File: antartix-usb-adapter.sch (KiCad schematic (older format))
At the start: 120 parts, among them IC1 FT2232D, J1 QTE-020-04-L-D-A, J2 0022232041, J3 614004185023, J4 WE_629105150521, J5 614004185023, J6 614004185023, U1 PCT2075GVX, U2 PAC1934T-I_JQ, U3 USB2514B-I_M2, U4 TPS2024DR, U5 TPS2024DR, U6 TPS2024DR, Y1 7C-24.000MBB-T, Y2 MQ-6.000-12-30_30_

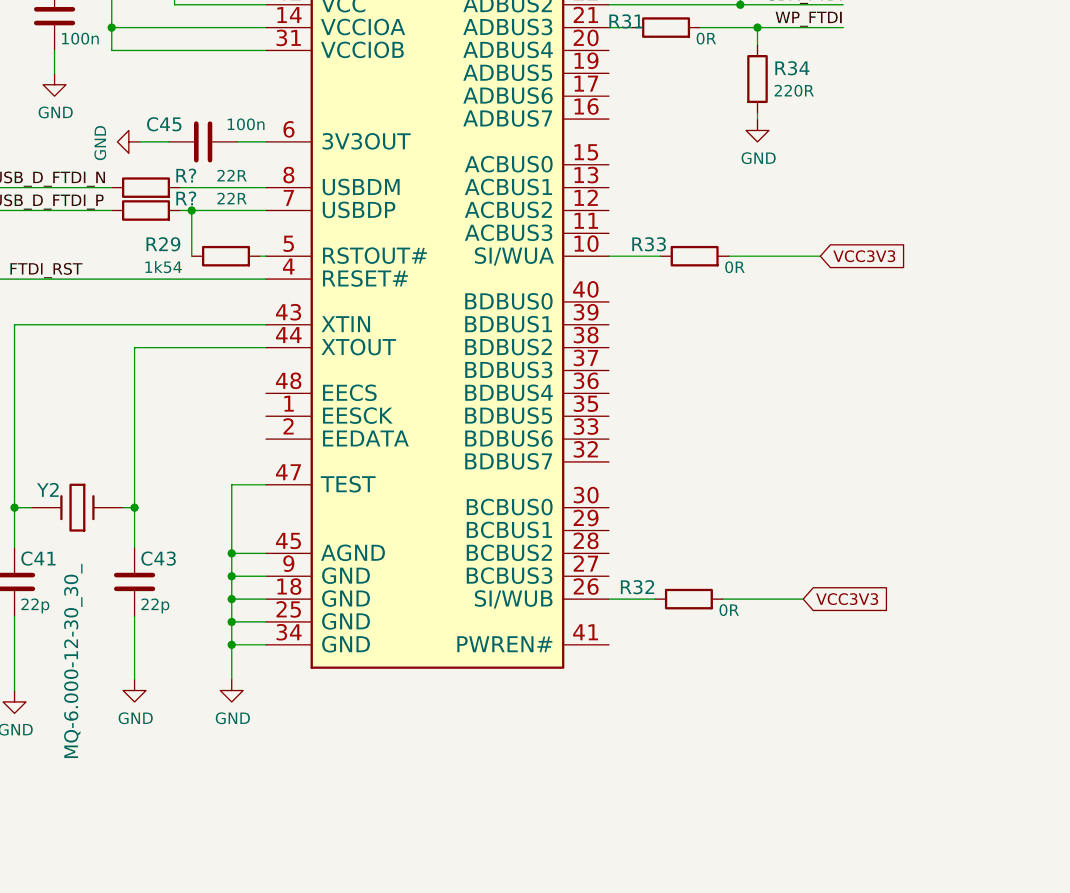
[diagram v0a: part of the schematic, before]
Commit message: Added micromatch-12 connector as PMOD GPIO. Bumped to 1.2.0
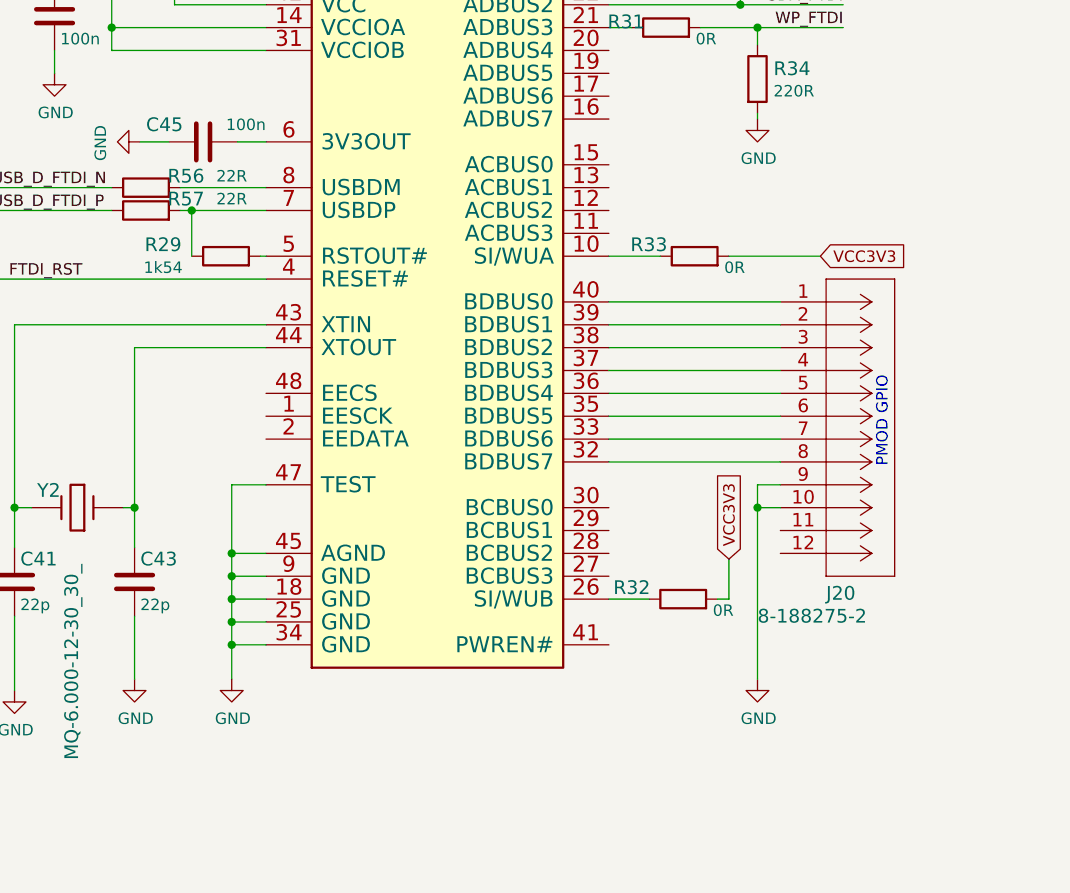
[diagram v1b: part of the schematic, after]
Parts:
- added J20: 8-188275-2, antartix-arty-controller-footprints:8-188275-2, symbol antartix-arty-controller:8-188275-2
- gave numbers to parts that had none: 2
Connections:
- net GND: now also J20.10, J20.9
- net at IC1.32 (BDBUS7): now also J20.8
- net at IC1.33 (BDBUS6): now also J20.7
- net at IC1.35 (BDBUS5): now also J20.6
- net at IC1.36 (BDBUS4): now also J20.5
- net at IC1.37 (BDBUS3): now also J20.4
- net at IC1.38 (BDBUS2): now also J20.3
- net at IC1.39 (BDBUS1): now also J20.2
- net at IC1.40 (BDBUS0): now also J20.1
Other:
- note added: "PMOD GPIO"
- moved on the sheet: R32
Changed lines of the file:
@@
 Title ""
 Date ""
-Rev ""
+Rev "1.2.0"
 Comp ""
 Comment1 ""
@@
 Wire Notes Line
 	11550 525  11550 11275
-Text GLabel 15575 9150 2    50   Input ~ 0
+Text GLabel 15250 8975 1    50   Input ~ 0
 VCC3V3
 Wire Wire Line
-	15225 9150 15575 9150
+	15250 9150 15250 8975
 $Comp
 L antartix-arty-controller:R_0R_0402 R?
 U 1 1 609392A5
-P 15075 9150
+P 15050 9150
 AR Path="/609392A5" Ref="R?"  Part="1"
 AR Path="/60924187/609392A5" Ref="R32"  Part="1"
-F 0 "R32" H 14850 9200 60  0000 C CNN
-F 1 "R_0R_0402" H 15075 9000 60  0001 C CNN
-F 2 "antartix-arty-controller-footprints:0402-res" H 15275 9350 60  0001 L CNN
-F 3 "" H 15075 9150 50  0001 C CNN
-F 4 "PANASONIC" H 15275 9550 60  0001 L CNN "Manufacturer"
-F 5 "ERJ2GE0R00X" H 15275 9450 60  0001 L CNN "MPN"
-F 6 "0R" H 15250 9100 50  0000 C CNN "Val"
-	1    15075 9150
+F 0 "R32" H 14825 9200 60  0000 C CNN
+F 1 "R_0R_0402" H 15050 9000 60  0001 C CNN
+F 2 "antartix-arty-controller-footprints:0402-res" H 15250 9350 60  0001 L CNN
+F 3 "" H 15050 9150 50  0001 C CNN
+F 4 "PANASONIC" H 15250 9550 60  0001 L CNN "Manufacturer"
+F 5 "ERJ2GE0R00X" H 15250 9450 60  0001 L CNN "MPN"
+F 6 "0R" H 15225 9100 50  0000 C CNN "Val"
+	1    15050 9150
 	1    0    0    -1
 $EndComp
 Wire Wire Line
-	14725 9150 14925 9150
+	14725 9150 14900 9150
 Text GLabel 9450 9225 1    50   Input ~ 0
 VCC3V3
@@
 P 12700 7350
 AR Path="/604C47E1/605E94E5" Ref="R?"  Part="1"
-AR Path="/60924187/605E94E5" Ref="R?"  Part="1"
-F 0 "R?" H 12875 7400 60  0000 C CNN
+AR Path="/60924187/605E94E5" Ref="R56"  Part="1"
+F 0 "R56" H 12875 7400 60  0000 C CNN
 F 1 "R_22R_0402" H 12700 7200 60  0001 C CNN
 F 2 "antartix-arty-controller-footprints:0402-res" H 12900 7550 60  0001 L CNN
@@
 P 12700 7450
 AR Path="/604C47E1/605E94EE" Ref="R?"  Part="1"
-AR Path="/60924187/605E94EE" Ref="R?"  Part="1"
-F 0 "R?" H 12875 7500 60  0000 C CNN
+AR Path="/60924187/605E94EE" Ref="R57"  Part="1"
+F 0 "R57" H 12875 7500 60  0000 C CNN
 F 1 "R_22R_0402" H 12700 7300 60  0001 C CNN
 F 2 "antartix-arty-controller-footprints:0402-res" H 12900 7650 60  0001 L CNN
@@
 Wire Wire Line
 	12550 7450 12025 7450
+$Comp
+L antartix-arty-controller:8-188275-2 J20
+U 1 1 6058E829
+P 15475 7850
+F 0 "J20" H 15675 6575 60  0000 L CNN
+F 1 "8-188275-2" H 15375 6475 60  0000 L CNN
+F 2 "antartix-arty-controller-footprints:8-188275-2" H 15875 7190 60  0001 C CNN
+F 3 "" H 15475 7850 60  0000 C CNN
+F 4 "8-188275-2" H 15850 8075 50  0001 C CNN "MPN"
+F 5 "TE Connectivity" H 15825 8000 50  0001 C CNN "Manufacturer"
+	1    15475 7850
+	1    0    0    -1
+$EndComp
+Wire Wire Line
+	14725 7850 15475 7850
+Wire Wire Line
+	14725 7950 15475 7950
+Wire Wire Line
+	14725 8050 15475 8050
+Wire Wire Line
+	14725 8150 15475 8150
+Wire Wire Line
+	14725 8250 15475 8250
+Wire Wire Line
+	14725 8350 15475 8350
+Wire Wire Line
+	14725 8450 15475 8450
+Wire Wire Line
+	14725 8550 15475 8550
+Wire Wire Line
+	15475 8650 15375 8650
+Wire Wire Line
+	15375 8650 15375 8750
+Wire Wire Line
+	15475 8750 15375 8750
+Connection ~ 15375 8750
+Wire Wire Line
+	15375 8750 15375 9500
+$Comp
+L antartix-arty-controller:GND #PWR?
+U 1 1 6084ADBB
+P 15375 9500
+AR Path="/6084ADBB" Ref="#PWR?"  Part="1"
+AR Path="/60924187/6084ADBB" Ref="#PWR0121"  Part="1"
+F 0 "#PWR0121" H 15375 9250 50  0001 C CNN
+F 1 "GND" H 15380 9327 50  0000 C CNN
+F 2 "" H 15375 9500 50  0001 C CNN
+F 3 "" H 15375 9500 50  0001 C CNN
+	1    15375 9500
+	1    0    0    -1
+$EndComp
+Wire Wire Line
+	15200 9150 15250 9150
+Text Notes 15950 8575 1    50   ~ 0
+PMOD GPIO
 $EndSCHEMATC

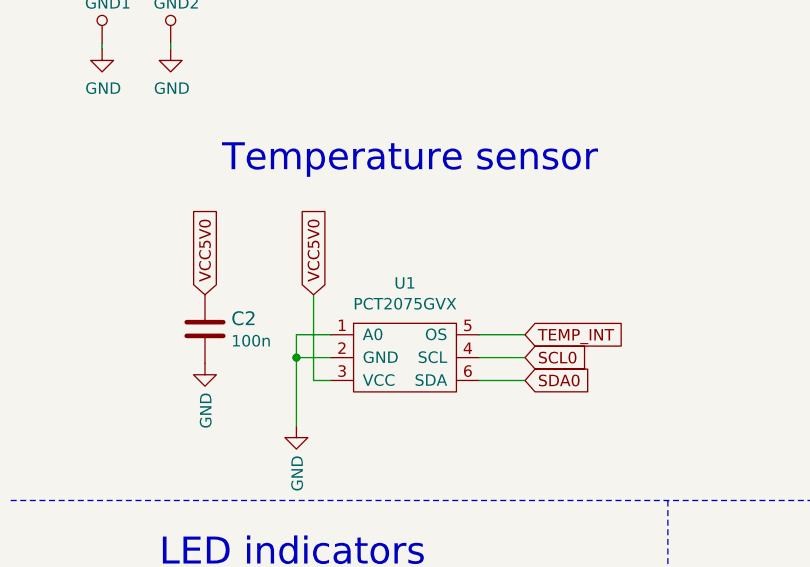
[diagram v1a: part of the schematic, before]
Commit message: Add MPNs
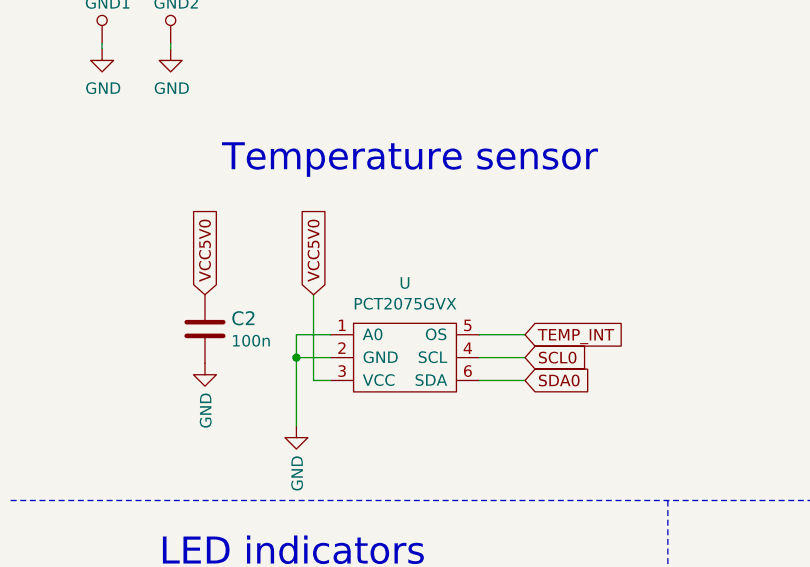
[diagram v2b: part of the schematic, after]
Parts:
- U: renamed from U1; MPN (none) -> PCT2075GVX; Manufacturer (none) -> NXP
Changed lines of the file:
@@
 Wire Wire Line
 	2525 5925 2725 5925
-$Comp
-L antartix-arty-controller:PCT2075GVX U?
-U 1 1 609395EB
-P 2225 6025
-AR Path="/609395EB" Ref="U?"  Part="1"
-AR Path="/60924187/609395EB" Ref="U1"  Part="1"
-F 0 "U1" H 2200 6350 50  0000 C CNN
-F 1 "PCT2075GVX" H 2200 6259 50  0000 C CNN
-F 2 "antartix-arty-controller-footprints:SOT95P275X110-6N" H 1925 6325 50  0001 C CNN
-F 3 "" H 1925 6325 50  0001 C CNN
-	1    2225 6025
-	1    0    0    -1
-$EndComp
 Wire Wire Line
 	2200 4025 2200 3900
@@
 Text Notes 15950 8575 1    50   ~ 0
 PMOD GPIO
+$Comp
+L antartix-arty-controller:PCT2075GVX U?
+U 1 1 609395EB
+P 2225 6025
+AR Path="/609395EB" Ref="U?"  Part="1"
+AR Path="/60924187/609395EB" Ref="U"  Part="1"
+F 0 "U" H 2200 6350 50  0000 C CNN
+F 1 "PCT2075GVX" H 2200 6259 50  0000 C CNN
+F 2 "antartix-arty-controller-footprints:SOT95P275X110-6N" H 1925 6325 50  0001 C CNN
+F 3 "" H 1925 6325 50  0001 C CNN
+F 4 "PCT2075GVX" H 2225 6025 50  0001 C CNN "MPN"
+F 5 "NXP" H 2225 6025 50  0001 C CNN "Manufacturer"
+	1    2225 6025
+	1    0    0    -1
+$EndComp
 $EndSCHEMATC

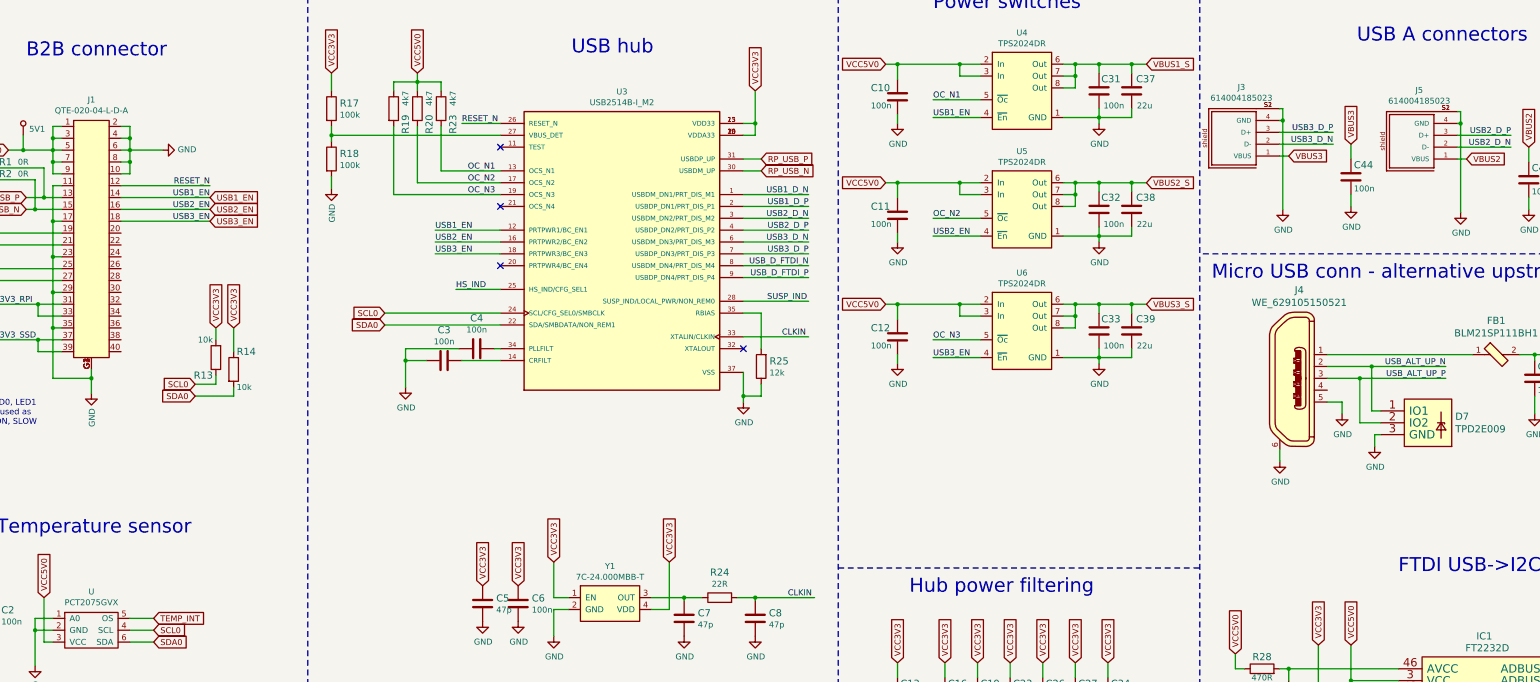
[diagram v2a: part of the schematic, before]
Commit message: Update libraries fields
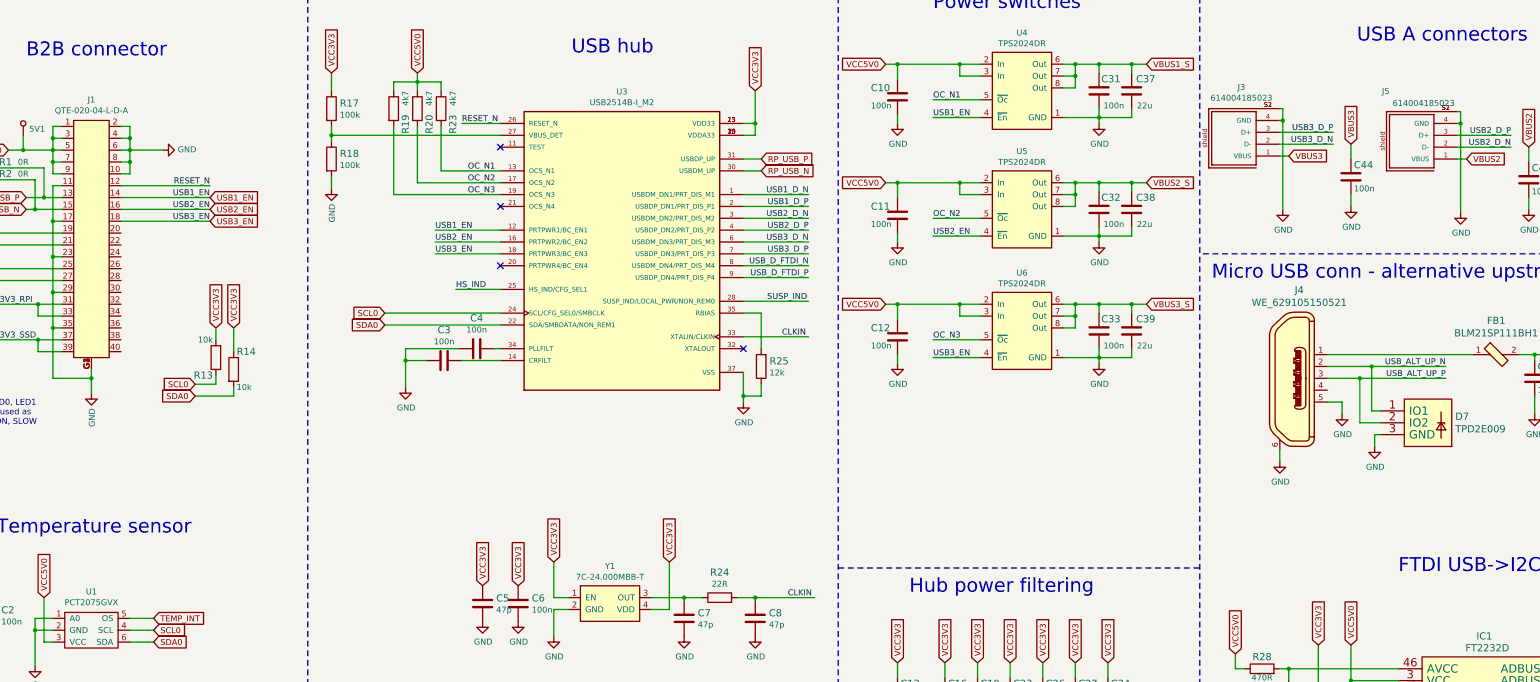
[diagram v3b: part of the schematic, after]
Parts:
- IC1: MPN (none) -> FT2232D-REEL; Manufacturer (none) -> FTDI
- J3, J5, J6: MPN (none) -> 614004185023; Manufacturer (none) -> WURTH ELEKTRONIK
- U3: MPN (none) -> USB2514B-I/M2; Manufacturer (none) -> Microchip
- renumbered U to U1
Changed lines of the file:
@@
 F 2 "antartix-arty-controller-footprints:QFN50P600X600X100-37N" H 5850 1900 50  0001 L BNN
 F 3 "" H 7350 3050 50  0001 L BNN
+F 4 "USB2514B-I/M2" H 7350 3050 50  0001 C CNN "MPN"
+F 5 "Microchip" H 7350 3050 50  0001 C CNN "Manufacturer"
 	1    7350 3050
 	1    0    0    -1
@@
 Wire Wire Line
 	12225 2025 12300 2025
-$Comp
-L antartix-arty-controller:614004185023 J?
-U 1 1 609390AE
-P 11825 1925
-AR Path="/609390AE" Ref="J?"  Part="1"
-AR Path="/60924187/609390AE" Ref="J3"  Part="1"
-F 0 "J3" H 11749 1444 50  0000 C CNN
-F 1 "614004185023" H 11749 1535 50  0000 C CNN
-F 2 "614004185023" H 11825 1925 50  0001 L BNN
-F 3 "" H 11825 1925 50  0001 L BNN
-	1    11825 1925
-	-1   0    0    1
-$EndComp
 Wire Wire Line
 	12225 1625 12250 1625
@@
 	1    0    0    -1
 $EndComp
-$Comp
-L antartix-arty-controller:614004185023 J?
-U 1 1 609390E8
-P 13325 1950
-AR Path="/609390E8" Ref="J?"  Part="1"
-AR Path="/60924187/609390E8" Ref="J5"  Part="1"
-F 0 "J5" H 13249 1469 50  0000 C CNN
-F 1 "614004185023" H 13249 1560 50  0000 C CNN
-F 2 "614004185023" H 13325 1950 50  0001 L BNN
-F 3 "" H 13325 1950 50  0001 L BNN
-	1    13325 1950
-	-1   0    0    1
-$EndComp
 Wire Wire Line
 	13725 1650 13750 1650
@@
 	15175 1650 15200 1650
 $Comp
-L antartix-arty-controller:614004185023 J?
-U 1 1 609391B6
-P 14775 1950
-AR Path="/609391B6" Ref="J?"  Part="1"
-AR Path="/60924187/609391B6" Ref="J6"  Part="1"
-F 0 "J6" H 14699 1469 50  0000 C CNN
-F 1 "614004185023" H 14699 1560 50  0000 C CNN
-F 2 "614004185023" H 14775 1950 50  0001 L BNN
-F 3 "" H 14775 1950 50  0001 L BNN
-	1    14775 1950
-	-1   0    0    1
-$EndComp
-$Comp
 L antartix-arty-controller:R_470R_0402 R?
 U 1 1 609391BF
@@
 Text Label 15750 6350 2    50   ~ 0
 SCL_FTDI
-$Comp
-L antartix-arty-controller:FT2232D IC?
-U 1 1 60939468
-P 13925 8150
-AR Path="/60939468" Ref="IC?"  Part="1"
-AR Path="/60924187/60939468" Ref="IC1"  Part="1"
-F 0 "IC1" H 13950 10225 60  0000 C CNN
-F 1 "FT2232D" H 13975 10125 60  0000 C CNN
-F 2 "antartix-arty-controller-footprints:LQFP-48_7x7mm" H 13975 10133 60  0001 C CNN
-F 3 "" H 13925 8150 60  0001 C CNN
-	1    13925 8150
-	1    0    0    -1
-$EndComp
 Text Notes 12875 1075 0    118  ~ 0
 USB A connectors
@@
 P 2225 6025
 AR Path="/609395EB" Ref="U?"  Part="1"
-AR Path="/60924187/609395EB" Ref="U"  Part="1"
-F 0 "U" H 2200 6350 50  0000 C CNN
+AR Path="/60924187/609395EB" Ref="U1"  Part="1"
+F 0 "U1" H 2200 6350 50  0000 C CNN
 F 1 "PCT2075GVX" H 2200 6259 50  0000 C CNN
 F 2 "antartix-arty-controller-footprints:SOT95P275X110-6N" H 1925 6325 50  0001 C CNN
@@
 	1    0    0    -1
 $EndComp
+$Comp
+L antartix-arty-controller:614004185023 J?
+U 1 1 609390AE
+P 11825 1925
+AR Path="/609390AE" Ref="J?"  Part="1"
+AR Path="/60924187/609390AE" Ref="J3"  Part="1"
+F 0 "J3" H 11749 1444 50  0000 C CNN
+F 1 "614004185023" H 11749 1535 50  0000 C CNN
+F 2 "614004185023" H 11825 1925 50  0001 L BNN
+F 3 "" H 11825 1925 50  0001 L BNN
+F 4 "614004185023" H 11825 1925 50  0001 C CNN "MPN"
+F 5 "WURTH ELEKTRONIK" H 11825 1925 50  0001 C CNN "Manufacturer"
+	1    11825 1925
+	-1   0    0    1
+$EndComp
+$Comp
+L antartix-arty-controller:614004185023 J?
+U 1 1 609390E8
+P 13325 1950
+AR Path="/609390E8" Ref="J?"  Part="1"
+AR Path="/60924187/609390E8" Ref="J5"  Part="1"
+F 0 "J5" H 13500 1450 50  0000 L BNN
+F 1 "614004185023" H 12950 1550 50  0000 L BNN
+F 2 "614004185023" H 13325 1950 50  0001 L BNN
+F 3 "" H 13325 1950 50  0001 L BNN
+F 4 "614004185023" H 13325 1950 50  0001 C CNN "MPN"
+F 5 "WURTH ELEKTRONIK" H 13325 1950 50  0001 C CNN "Manufacturer"
+	1    13325 1950
+	-1   0    0    1
+$EndComp
+$Comp
+L antartix-arty-controller:614004185023 J?
+U 1 1 609391B6
+P 14775 1950
+AR Path="/609391B6" Ref="J?"  Part="1"
+AR Path="/60924187/609391B6" Ref="J6"  Part="1"
+F 0 "J6" H 14699 1469 50  0000 C CNN
+F 1 "614004185023" H 14699 1560 50  0000 C CNN
+F 2 "614004185023" H 14775 1950 50  0001 L BNN
+F 3 "" H 14775 1950 50  0001 L BNN
+F 4 "614004185023" H 14775 1950 50  0001 C CNN "MPN"
+F 5 "WURTH ELEKTRONIK" H 14775 1950 50  0001 C CNN "Manufacturer"
+	1    14775 1950
+	-1   0    0    1
+$EndComp
+$Comp
+L antartix-arty-controller:FT2232D IC?
+U 1 1 60939468
+P 13925 8150
+AR Path="/60939468" Ref="IC?"  Part="1"
+AR Path="/60924187/60939468" Ref="IC1"  Part="1"
+F 0 "IC1" H 13950 10225 60  0000 C CNN
+F 1 "FT2232D" H 13975 10125 60  0000 C CNN
+F 2 "antartix-arty-controller-footprints:LQFP-48_7x7mm" H 13975 10133 60  0001 C CNN
+F 3 "" H 13925 8150 60  0001 C CNN
+F 4 "FT2232D-REEL" H 13925 8150 50  0001 C CNN "MPN"
+F 5 "FTDI" H 13925 8150 50  0001 C CNN "Manufacturer"
+	1    13925 8150
+	1    0    0    -1
+$EndComp
